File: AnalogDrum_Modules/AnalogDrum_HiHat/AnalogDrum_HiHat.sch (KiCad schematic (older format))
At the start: 7 parts, among them J101 Conn_01x05_Male

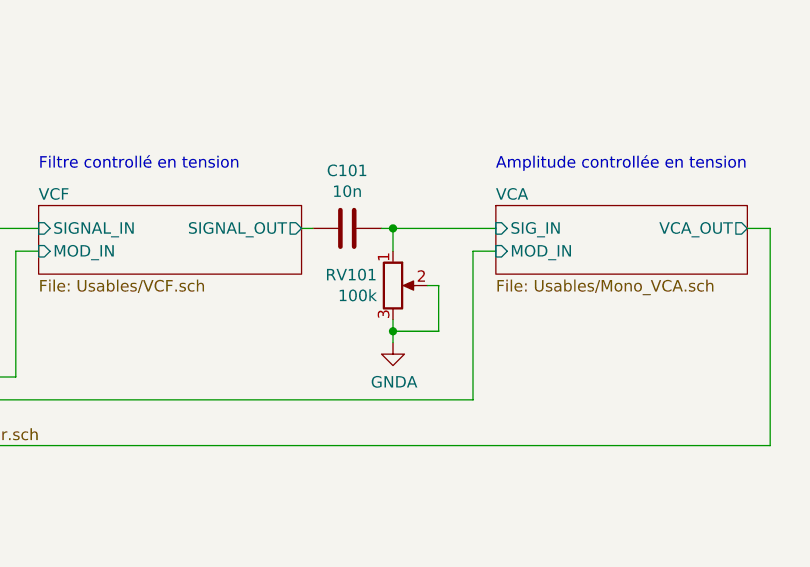
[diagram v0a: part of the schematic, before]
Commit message: Version 0.1.1
Corrections mineures :
- Vérification des potentiomètres
- Passage des connecteurs de carte e n JST
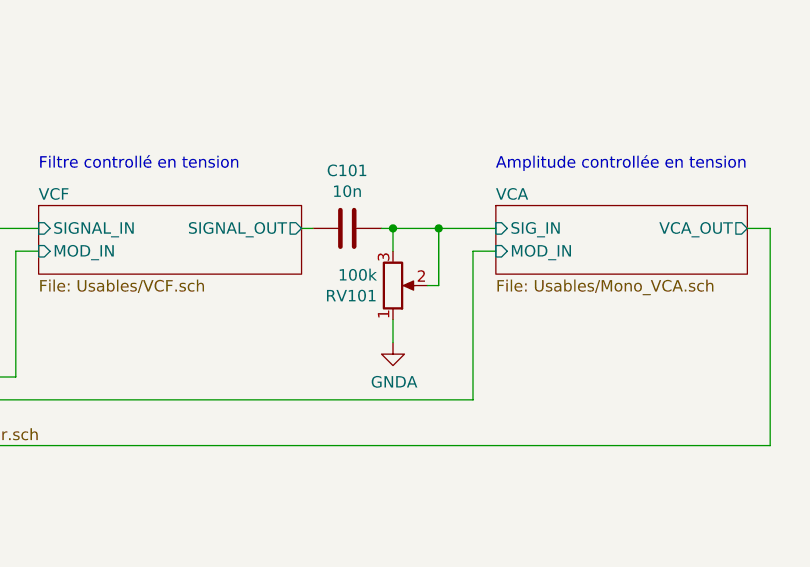
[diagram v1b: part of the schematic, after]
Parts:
- J101: footprint Connector_PinHeader_2.54mm:PinHeader_1x05_P2.54mm_Horizontal -> Connector_JST:JST_EH_B5B-EH-A_1x05_P2.50mm_Vertical
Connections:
- net GNDA: now also RV101.1; no longer RV101.2, RV101.3
- net VCA/SIG_IN: now also RV101.2, RV101.3; no longer RV101.1
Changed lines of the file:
@@
 F 3 "~" H 6750 3700 50  0001 C CNN
 	1    6750 3700
-	1    0    0    -1
+	1    0    0    1
 $EndComp
 Wire Wire Line
@@
 Connection ~ 6750 3450
 Wire Wire Line
-	6750 3450 7200 3450
+	6750 3450 6950 3450
 $Comp
 L power:GNDA #PWR0102
@@
 $EndComp
 Wire Wire Line
-	6750 3850 6750 3900
-Wire Wire Line
-	6750 3900 6950 3900
-Wire Wire Line
-	6950 3900 6950 3700
-Wire Wire Line
 	6950 3700 6900 3700
-Connection ~ 6750 3900
-Wire Wire Line
-	6750 3900 6750 3950
 Wire Wire Line
 	4850 3450 5200 3450
@@
 F 0 "J101" H 3308 4781 50  0000 C CNN
 F 1 "Conn_01x05_Male" H 3308 4690 50  0000 C CNN
-F 2 "Connector_PinHeader_2.54mm:PinHeader_1x05_P2.54mm_Horizontal" H 3200 4400 50  0001 C CNN
+F 2 "Connector_JST:JST_EH_B5B-EH-A_1x05_P2.50mm_Vertical" H 3200 4400 50  0001 C CNN
 F 3 "~" H 3200 4400 50  0001 C CNN
 	1    3200 4400
@@
 Text Notes 550  7700 0    50   ~ 0
 Réalisé par Lazare\nInspiré de la génération par la TR-808
+Wire Wire Line
+	6750 3850 6750 3950
+Wire Wire Line
+	6950 3700 6950 3450
+Connection ~ 6950 3450
+Wire Wire Line
+	6950 3450 7200 3450
 $EndSCHEMATC
